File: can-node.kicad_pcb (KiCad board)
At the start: 2 copper layers, 50 x 60 mm, 70 parts, among them P1 Debug, P2 SPI1, P3 CONN_01X04, P4 CONN_02X05, P5 CONN_02X05, Q1 DMP6023LSS, SW1 SW_PUSH, SW2 SW_PUSH, SW3 SW_PUSH, U1 LMR16006, U2 SN74LVC1G08, U3 STM32F072RB, U4 HDC1080, U5 TCAN334, X1 32.768KHz 12.5pF

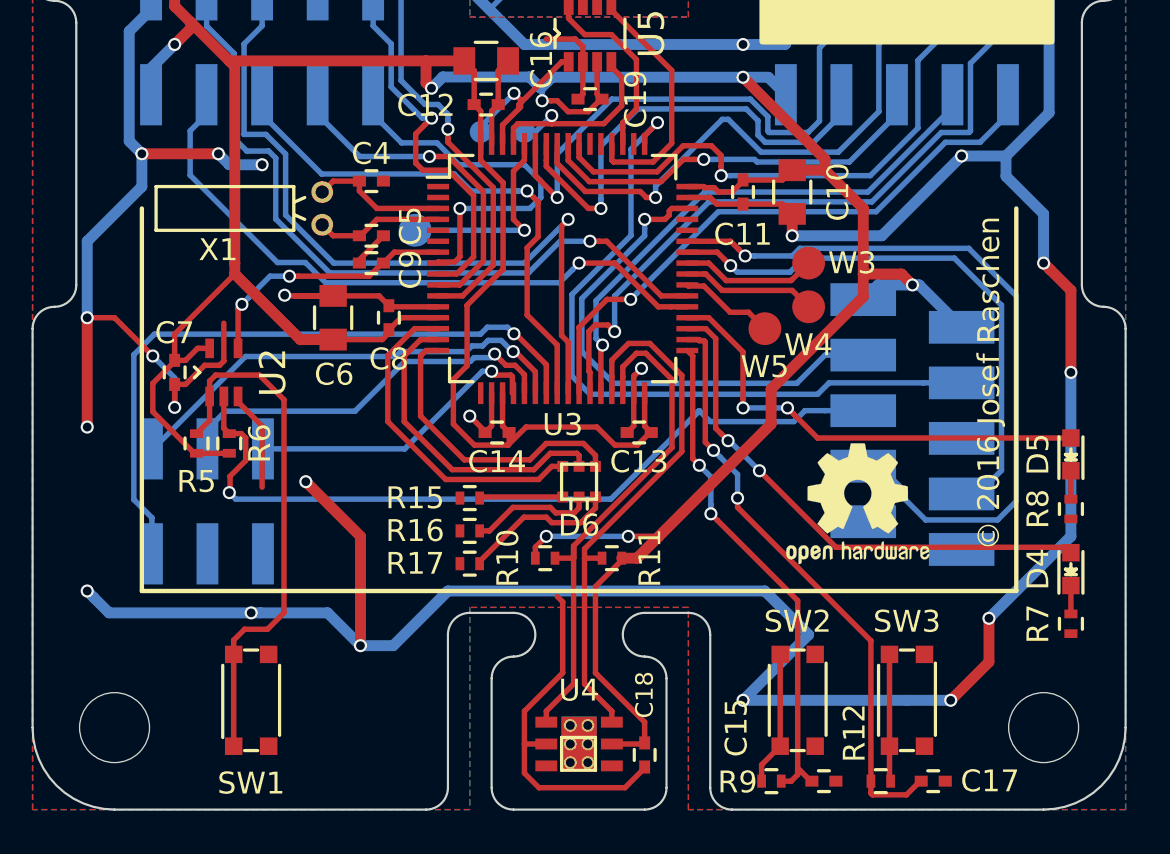
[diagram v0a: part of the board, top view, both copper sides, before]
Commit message: Add ambient light sensor, minor layout optimizations.
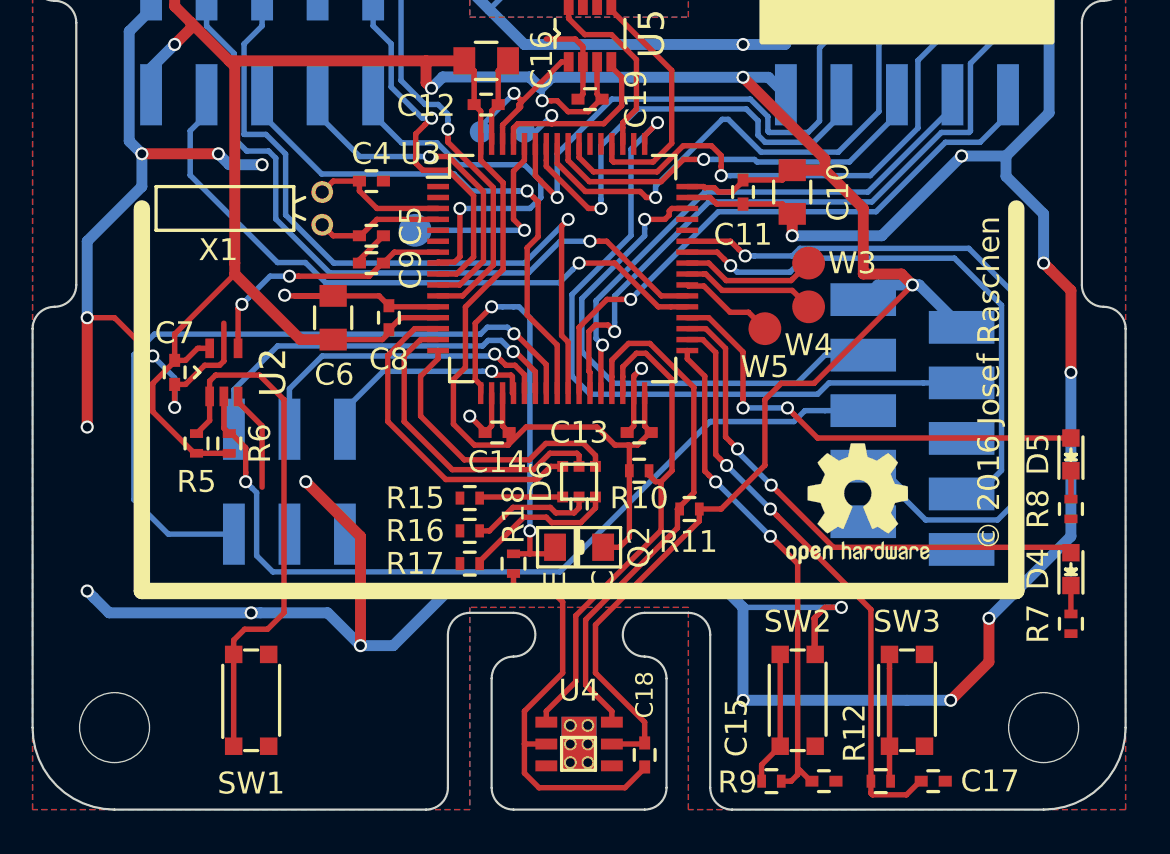
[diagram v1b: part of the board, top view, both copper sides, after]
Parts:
- added Q2: SFH3711, can-node:SFH3711, F.Cu at (145.0, 113.0)
- added R18: 4.7k, Resistors_SMD:R_0402, F.Cu at (142.0, 113.8)
- moved R10 5.87 mm to (147.8, 109.5)
- moved R11 4.20 mm to (150.1, 111.2)
- moved P2 3.86 mm to (131.8, 110.0)
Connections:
- U3 pad 17: Net-(U3-Pad17) -> /Microcontroller/ADC_IN3
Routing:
- net /Microcontroller/ADC_IN3: track 0.00 -> 19.1 mm, vias 0 -> 2
- net GND: track 422.3 -> 429.4 mm, vias 45 -> 46
- net Net-(P2-Pad2): track 13.8 -> 10.2 mm
- net Net-(P2-Pad4): track 18.1 -> 14.5 mm
- net Net-(P2-Pad6): track 21.2 -> 18.1 mm
- net Net-(P2-Pad5): track 30.9 -> 33.3 mm
- net Net-(P1-Pad5): track 37.0 -> 39.3 mm
- net +3.3VADC: track 195.2 -> 195.9 mm, vias 7 -> 5
- net Net-(R10-Pad2): track 23.7 -> 23.1 mm
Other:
- board text added: "24V DC"
- board text added: "CANH"
- board text added: "CANL"
- board text added: "GND"

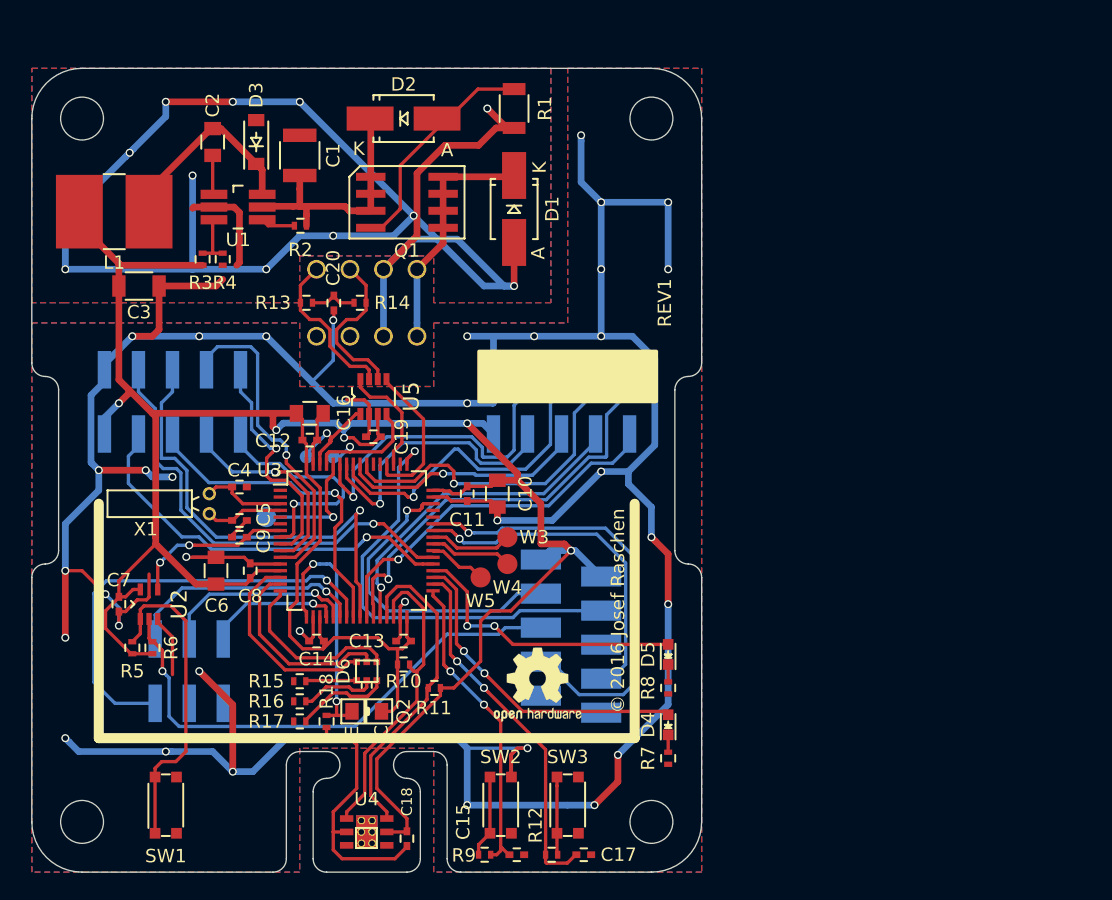
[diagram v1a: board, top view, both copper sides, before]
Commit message: Some modifications to schematic, BOM, start releayout
- add LED display
- change crystal for RTC
- use components that are available at some distributors
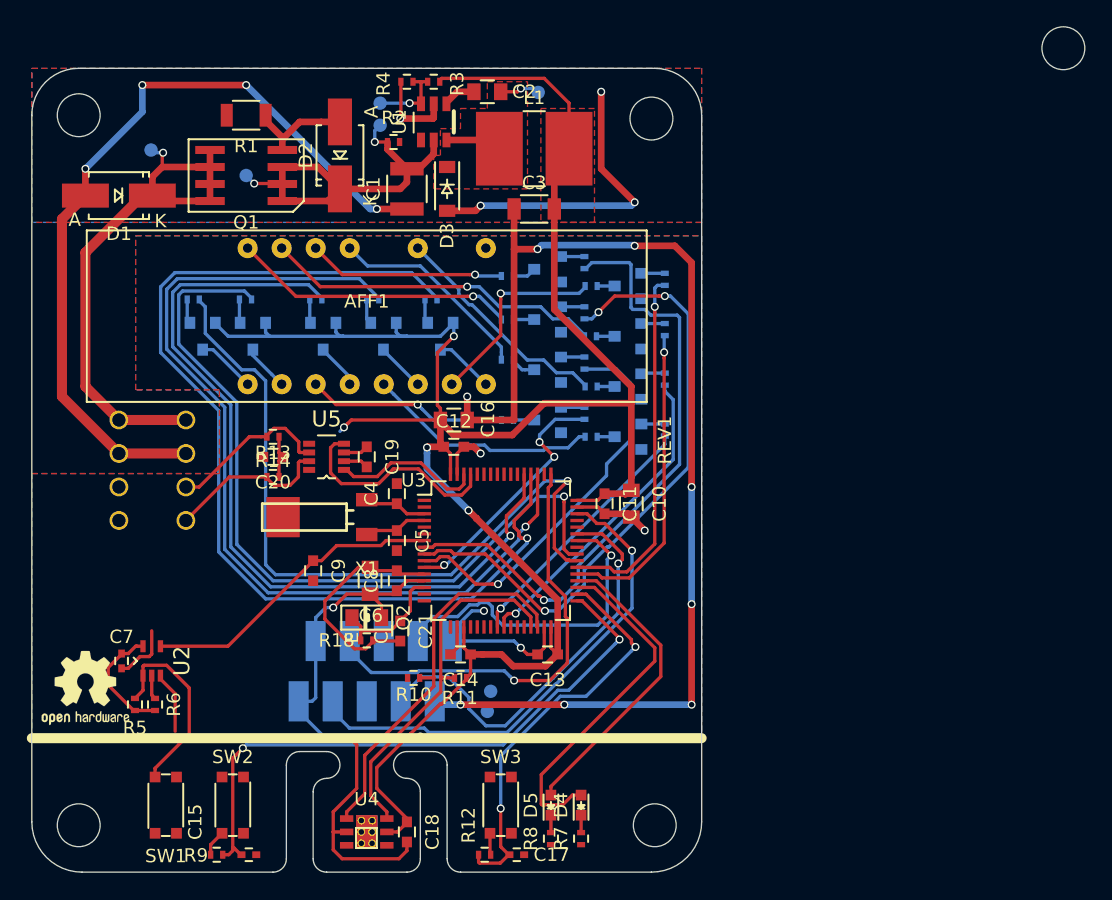
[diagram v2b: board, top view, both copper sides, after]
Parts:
- removed D6: LED_RGB_EP, CAN_Node:Everlight_19-337
- removed P2: SPI1, can-node:PIN_Header_SMD_2.54mm_02x03
- removed P4, P5: CONN_02X05, CAN_Node:PIN_Header_SMD_2.54mm_02x05
- removed W1: CAN_TX, can-node:Measurement_Point_tiny
- removed W2: CAN_RX, can-node:Measurement_Point_tiny
- removed W3: PA8, Measurement_Points:Measurement_Point_Round-SMD-Pad_Small
- removed W4: PC9, Measurement_Points:Measurement_Point_Round-SMD-Pad_Small
- removed W5: PC8, Measurement_Points:Measurement_Point_Round-SMD-Pad_Small
- removed W6: BOOT0, Measurement_Points:Measurement_Point_Round-SMD-Pad_Small
- added AFF1: LTC-4627, can-node:LTC-4627, F.Cu at (145.0, 83.5)
- added C21: 100n, Capacitors_SMD:C_0603, F.Cu at (147.5, 107.0)
- added Q10: BC807-40, TO_SOT_Packages_SMD:SOT-23, B.Cu at (150.5, 85.0)
- added Q11: BC807-40, TO_SOT_Packages_SMD:SOT-23, B.Cu at (141.8, 85.0)
- added Q12: BC817-40, TO_SOT_Packages_SMD:SOT-23, B.Cu at (164.5, 92.5)
- added Q13: BC817-40, TO_SOT_Packages_SMD:SOT-23, B.Cu at (164.5, 88.8)
- added Q14: BC817-40, TO_SOT_Packages_SMD:SOT-23, B.Cu at (164.5, 85.0)
- added Q15: BC817-40, TO_SOT_Packages_SMD:SOT-23, B.Cu at (164.5, 81.2)
- added Q3: BC817-40, TO_SOT_Packages_SMD:SOT-23, B.Cu at (158.5, 80.0)
- added Q4: BC807-40, TO_SOT_Packages_SMD:SOT-23, B.Cu at (132.8, 85.0)
- added Q5: BC817-40, TO_SOT_Packages_SMD:SOT-23, B.Cu at (158.5, 83.8)
- added Q6: BC807-40, TO_SOT_Packages_SMD:SOT-23, B.Cu at (136.5, 85.0)
- added Q7: BC817-40, TO_SOT_Packages_SMD:SOT-23, B.Cu at (158.5, 87.5)
- added Q8: BC807-40, TO_SOT_Packages_SMD:SOT-23, B.Cu at (146.2, 85.0)
- added Q9: BC817-40, TO_SOT_Packages_SMD:SOT-23, B.Cu at (158.5, 91.2)
- added R19: 1k, Resistors_SMD:R_0402, B.Cu at (161.2, 90.8)
- added R20: 1k, Resistors_SMD:R_0402, B.Cu at (141.2, 82.2)
- added R21: 1k, Resistors_SMD:R_0402, B.Cu at (149.8, 82.2)
- added R22: 1k, Resistors_SMD:R_0402, B.Cu at (145.4, 82.2)
- added R23: 1k, Resistors_SMD:R_0402, B.Cu at (135.9, 82.2)
- added R24: 1k, Resistors_SMD:R_0402, B.Cu at (132.1, 82.2)
- added R25: 120, Resistors_SMD:R_0402, B.Cu at (155.5, 80.5)
- added R26: 120, Resistors_SMD:R_0402, B.Cu at (155.5, 83.8)
- added R27: 120, Resistors_SMD:R_0402, B.Cu at (155.5, 86.8)
- added R28: 120, Resistors_SMD:R_0402, B.Cu at (155.5, 91.2)
- added R29: 1k, Resistors_SMD:R_0402, B.Cu at (167.2, 92.0)
- added R30: 1k, Resistors_SMD:R_0402, B.Cu at (167.2, 88.2)
- added R31: 1k, Resistors_SMD:R_0402, B.Cu at (167.2, 84.5)
- added R32: 1k, Resistors_SMD:R_0402, B.Cu at (167.2, 80.8)
- added R33: 120, Resistors_SMD:R_0402, B.Cu at (161.8, 92.5)
- added R34: 120, Resistors_SMD:R_0402, B.Cu at (161.8, 88.8)
- added R35: 120, Resistors_SMD:R_0402, B.Cu at (161.7, 85.0)
- added R36: 120, Resistors_SMD:R_0402, B.Cu at (161.8, 81.2)
- added REF**: MountingHole_3.2mm_M3, Mounting_Holes:MountingHole_3.2mm_M3, F.Cu at (197.0, 63.5)
- added REF***: OSHW-Logo2_7.3x6mm_SilkScreen, Symbols:OSHW-Logo2_7.3x6mm_SilkScreen, B.Cu at (156.8, 110.5)
- added W10: FB, can-node:Measurement_Point_tiny, B.Cu at (146.0, 67.6)
- added W11: SW, can-node:Measurement_Point_tiny, B.Cu at (157.8, 66.8)
- added W16: SDA, can-node:Measurement_Point_tiny, B.Cu at (154.2, 111.5)
- added W17: SCL, can-node:Measurement_Point_tiny, B.Cu at (154.0, 113.0)
- added W7: VINA, can-node:Measurement_Point_tiny, B.Cu at (128.9, 71.1)
- added W8: VINB, can-node:Measurement_Point_tiny, B.Cu at (136.0, 73.0)
- added W9: VINC, can-node:Measurement_Point_tiny, B.Cu at (146.0, 69.2)
- C11, C12, C13, C14, C18, C19, C20, C4, C5, C8, C9: footprint Capacitors_SMD:C_0402 -> Capacitors_SMD:C_0603
- C2: value 100n 100V -> 100n >10V
- R15, R16, R17: value 220 -> 1k; moved to B.Cu
- U1: footprint TO_SOT_Packages_SMD:TSOT-6-MK06A_Handsoldering -> can-node:TI-DDC
- X1: footprint CAN_Node:Crystal_DT-26 -> can-node:Crystal-MS1V-T1K
- moved R15 37.8 mm to (161.2, 79.5), turned to 270 degrees
- moved R16 36.0 mm to (161.2, 83.2), turned to 270 degrees
- moved R17 34.2 mm to (161.2, 87.0), turned to 270 degrees
- moved REF*** 33.8 mm to (124.0, 111.2)
- moved L1 31.7 mm to (157.5, 71.0), turned to 0 degrees
- moved C3 30.1 mm to (157.5, 75.5), turned to 180 degrees
- moved D1 29.5 mm to (126.5, 74.5), turned to 180 degrees
- moved R3 21.8 mm to (150.0, 66.0), turned to 180 degrees
- moved C2 20.8 mm to (154.0, 66.8), turned to 180 degrees
- moved P3 20.3 mm to (129.0, 95.0), turned to 270 degrees
- moved R1 20.0 mm to (136.0, 68.5), turned to 180 degrees
- moved C15 20.0 mm to (136.2, 123.7)
- moved R9 20.0 mm to (133.8, 123.7)
- moved SW2 20.0 mm to (135.0, 120.0)
- moved R4 19.1 mm to (148.0, 66.0), turned to 180 degrees
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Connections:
- net CAN_RX renamed Net-(U3-Pad61)
- net CAN_TX renamed Net-(U3-Pad62)
- Q2 pad 2: /Microcontroller/ADC_IN3 -> /Microcontroller/ADC_IN0
- R15 pad 2: GND -> PC0
- R16 pad 2: GND -> PC1
- R17 pad 2: GND -> PC2
- R18 pad 1: /Microcontroller/ADC_IN3 -> /Microcontroller/ADC_IN0
- U3 pad 10: /Microcontroller/PC2 -> PC2
- U3 pad 11: /Microcontroller/PC3 -> PC3
- U3 pad 14: Net-(D6-Pad6) -> /Microcontroller/ADC_IN0
- U3 pad 17: /Microcontroller/ADC_IN3 -> Net-(U3-Pad17)
- U3 pad 24: /Microcontroller/PC4 -> PC4
- U3 pad 25: /Microcontroller/PC5 -> PC5
- U3 pad 37: /Microcontroller/PC6 -> PC6
- U3 pad 38: /Microcontroller/PC7 -> PC7
- U3 pad 39: Net-(U3-Pad39) -> PC8
- U3 pad 40: Net-(U3-Pad40) -> PC9
- U3 pad 51: CAN_STANDBY -> PC10
- U3 pad 52: CAN_SHUTDOWN -> PC11
- U3 pad 53: Net-(U3-Pad53) -> PC12
- U3 pad 8: /Microcontroller/PC0 -> PC0
- U3 pad 9: /Microcontroller/PC1 -> PC1
- U5 pad 5: CAN_SHUTDOWN -> Net-(U3-Pad44)
- U5 pad 8: CAN_STANDBY -> Net-(U3-Pad45)
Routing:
- net GND: track 429.4 -> 246.4 mm, vias 46 -> 20
- net PC11: track 0.00 -> 76.0 mm, vias 0 -> 1
- net PC10: track 0.00 -> 68.5 mm, vias 0 -> 1
- net PC12: track 0.00 -> 61.6 mm, vias 0 -> 1
- net PC9: track 0.00 -> 59.5 mm, vias 0 -> 1
- net PC8: track 0.00 -> 55.7 mm, vias 0 -> 1
- net PC0: track 0.00 -> 47.6 mm, vias 0 -> 1
- net PC1: track 0.00 -> 47.2 mm, vias 0 -> 3
- net Net-(P1-Pad5): track 39.3 -> 1.90 mm, vias 1 -> 0
- net /Microcontroller/PC5: track 34.9 -> 0.00 mm, vias 1 -> 0
- net /Microcontroller/PC7: track 33.9 -> 0.00 mm, vias 1 -> 0
- net Net-(P2-Pad5): track 33.3 -> 0.00 mm, vias 1 -> 0
- net /Microcontroller/PB1: track 32.5 -> 0.00 mm, vias 1 -> 0
- net /Microcontroller/PC6: track 30.0 -> 0.00 mm, vias 1 -> 0
- net PC2: track 0.00 -> 29.5 mm, vias 0 -> 1
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- added copper zone on F.Cu, net +3.3VADC
- added copper zone on F.Cu, net Net-(C2-Pad1)
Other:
- outline, holes or cut-outs redrawn
- board text added: "+3.3V"
- board text added: "0V"
- board text added: "SWCLK"
- board text added: "SWDIO"
- board text added: "UART_RX"
- board text added: "UART_TX"
- board text added: "© 2017 Josef Raschen"
- board text removed: "GND"
- board text removed: "© 2016 Josef Raschen"

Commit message: Layouting work
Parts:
- removed R15, R16, R17, R19, R20, R21, R22, R23, R24, R29, R30, R31, R32: 1k, Resistors_SMD:R_0402
- removed the REF** at (197.0, 63.5)
- added P2: SPI1, can-node:PIN_Header_SMD_2.54mm_02x03, B.Cu at (142.7, 108.0)
- added W1: CAN_TX, can-node:Measurement_Point_tiny, F.Cu at (146.8, 93.2)
- added W12: +3.3V, can-node:Measurement_Point_tiny, B.Cu at (160.8, 79.8)
- added W18: LSENS, can-node:Measurement_Point_tiny, B.Cu at (152.4, 103.4)
- added W2: CAN_RX, can-node:Measurement_Point_tiny, F.Cu at (143.0, 97.0)
- added W3: PA8, can-node:Measurement_Point_tiny, F.Cu at (162.3, 101.9)
- added W6: BOOT0, can-node:Measurement_Point_tiny, F.Cu at (154.7, 93.7)
- Q10, Q4, Q6, Q8: value BC807-40 -> BSS138
- Q11: value BC807-40 -> BSS84P
- Q12, Q13, Q14, Q15: value BC817-40 -> BSS84P
- Q3, Q5, Q7, Q9: value BC817-40 -> BSS138
- moved Q3 27.4 mm to (131.2, 82.8), turned to 0 degrees
- moved Q5 27.4 mm to (131.2, 86.2), turned to 0 degrees
- moved Q12 26.6 mm to (138.8, 85.8), turned to 270 degrees
- moved Q9 25.9 mm to (134.8, 81.0), turned to 0 degrees
- moved R35 24.8 mm to (137.4, 80.0), turned to 180 degrees
- moved P1 23.2 mm to (162.8, 95.0), turned to 270 degrees
- moved R26 22.1 mm to (134.0, 78.5), turned to 180 degrees
- moved Q15 21.2 mm to (143.8, 85.8), turned to 270 degrees
- moved R34 17.8 mm to (147.0, 78.8), turned to 270 degrees
- moved R33 16.6 mm to (146.2, 86.5), turned to 90 degrees
- moved Q13 16.0 mm to (148.8, 85.8), turned to 270 degrees
- moved R28 15.0 mm to (141.2, 86.5), turned to 90 degrees
- moved R25 14.8 mm to (140.8, 80.0), turned to 180 degrees
- moved R27 13.4 mm to (143.8, 80.3), turned to 270 degrees
- moved Q7 13.2 mm to (146.2, 82.5), turned to 270 degrees
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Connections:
- Q10 pad 1: Net-(Q10-Pad1) -> PC7
- Q10 pad 2: +3.3VADC -> GND
- Q10 pad 3: Net-(AFF1-Pad8) -> Net-(Q10-Pad3)
- Q11 pad 1: Net-(Q11-Pad1) -> PC8
- Q11 pad 3: Net-(AFF1-Pad4) -> Net-(AFF1-Pad1)
- Q12 pad 1: Net-(Q12-Pad1) -> PC9
- Q12 pad 2: GND -> +3.3VADC
- Q12 pad 3: Net-(Q12-Pad3) -> Net-(AFF1-Pad2)
- Q13 pad 1: Net-(Q13-Pad1) -> PC10
- Q13 pad 2: GND -> +3.3VADC
- Q13 pad 3: Net-(Q13-Pad3) -> Net-(AFF1-Pad6)
- Q14 pad 1: Net-(Q14-Pad1) -> PC11
- Q14 pad 2: GND -> +3.3VADC
- Q14 pad 3: Net-(Q14-Pad3) -> Net-(AFF1-Pad8)
- Q15 pad 1: Net-(Q15-Pad1) -> PC12
- Q15 pad 2: GND -> +3.3VADC
- Q15 pad 3: Net-(Q15-Pad3) -> Net-(AFF1-Pad4)
- Q3 pad 1: Net-(Q3-Pad1) -> PC0
- Q4 pad 1: Net-(Q4-Pad1) -> PC1
- Q4 pad 2: +3.3VADC -> GND
- Q4 pad 3: Net-(AFF1-Pad1) -> Net-(Q4-Pad3)
- Q5 pad 1: Net-(Q5-Pad1) -> PC2
- Q6 pad 1: Net-(Q6-Pad1) -> PC3
- Q6 pad 2: +3.3VADC -> GND
- Q6 pad 3: Net-(AFF1-Pad2) -> Net-(Q6-Pad3)
- Q7 pad 1: Net-(Q7-Pad1) -> PC4
- Q8 pad 1: Net-(Q8-Pad1) -> PC5
- Q8 pad 2: +3.3VADC -> GND
- Q8 pad 3: Net-(AFF1-Pad6) -> Net-(Q8-Pad3)
- Q9 pad 1: Net-(Q9-Pad1) -> PC6
- R26 pad 2: Net-(Q5-Pad3) -> Net-(Q4-Pad3)
- R27 pad 2: Net-(Q7-Pad3) -> Net-(Q5-Pad3)
- R28 pad 2: Net-(Q9-Pad3) -> Net-(Q6-Pad3)
- R33 pad 2: Net-(Q12-Pad3) -> Net-(Q7-Pad3)
- R34 pad 2: Net-(Q13-Pad3) -> Net-(Q8-Pad3)
- R35 pad 2: Net-(Q14-Pad3) -> Net-(Q9-Pad3)
- R36 pad 2: Net-(Q15-Pad3) -> Net-(Q10-Pad3)
- U3 pad 15: Net-(U3-Pad15) -> /Microcontroller/PA1
- U3 pad 16: Net-(U3-Pad16) -> /Microcontroller/PA2
- U5 pad 5: Net-(U3-Pad44) -> /Microcontroller/PA1
- U5 pad 8: Net-(U3-Pad45) -> /Microcontroller/PA2
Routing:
- net GND: track 246.4 -> 393.3 mm, vias 20 -> 36
- net +3.3VADC: track 200.3 -> 275.0 mm, vias 6 -> 12
- net Net-(P1-Pad5): track 1.90 -> 68.7 mm, vias 0 -> 1
- net PC11: track 76.0 -> 13.3 mm
- net PC10: track 68.5 -> 18.0 mm
- net PC12: track 61.6 -> 25.6 mm
- net /Microcontroller/PA1: track 0.00 -> 29.8 mm
- net /Microcontroller/PA2: track 0.00 -> 28.6 mm
- net /Microcontroller/UART1_RX: track 31.3 -> 3.56 mm
- net PC9: track 59.5 -> 33.4 mm
- net /Microcontroller/SWCLK: track 33.3 -> 8.18 mm
- net Net-(AFF1-Pad15): track 25.4 -> 1.89 mm, vias 1 -> 0
- net Net-(P2-Pad6): track 0.00 -> 21.8 mm, vias 0 -> 1
- net /Microcontroller/SWDIO: track 37.1 -> 15.5 mm
- net /Microcontroller/UART1_TX: track 24.7 -> 4.90 mm
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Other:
- board text removed: "+3.3V"
- board text removed: "SWCLK"
- board text removed: "SWDIO"
- board text removed: "UART_RX"
- board text removed: "UART_TX"

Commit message: Remove spi connector.
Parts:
- removed P2: SPI1, can-node:PIN_Header_SMD_2.54mm_02x03
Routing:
- net GND: track 393.3 -> 339.1 mm, vias 36 -> 30
- net +3.3VADC: track 275.0 -> 235.0 mm
- net Net-(U3-Pad22): track 21.8 -> 0.00 mm, vias 1 -> 0
- net Net-(U3-Pad23): track 17.1 -> 0.00 mm, vias 1 -> 0
- net Net-(U3-Pad20): track 10.8 -> 0.00 mm, vias 1 -> 0
- net Net-(U3-Pad21): track 9.86 -> 0.00 mm, vias 1 -> 0
- net /Microcontroller/PA1: track 29.8 -> 31.1 mm
